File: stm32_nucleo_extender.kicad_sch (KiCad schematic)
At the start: 7 parts, among them CN10 6-534206-9, CN7 6-534206-9, J1 TBL009-254-20GY-2GY, J2 TBL009-254-20GY-2GY, J3 TBL009-254-20GY-2GY, J4 TBL009-254-20GY-2GY, U1 NUCLEO-F446RE

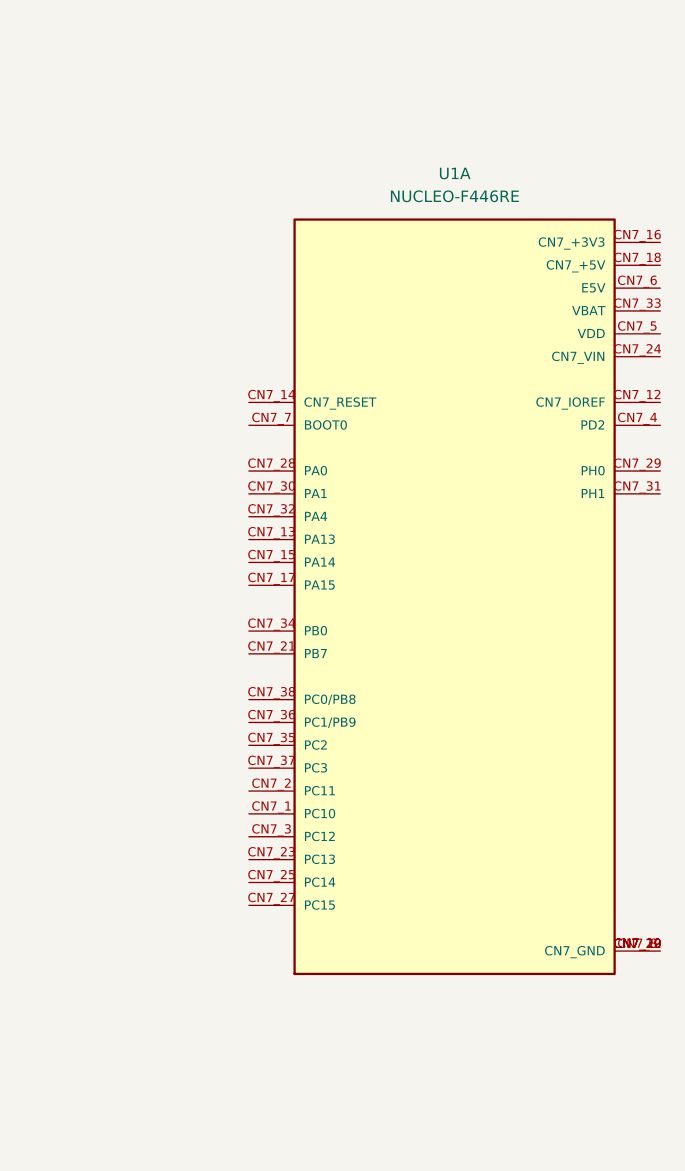
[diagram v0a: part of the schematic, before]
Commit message: [UPD] to kicad 10.0 [ADD] round tracks
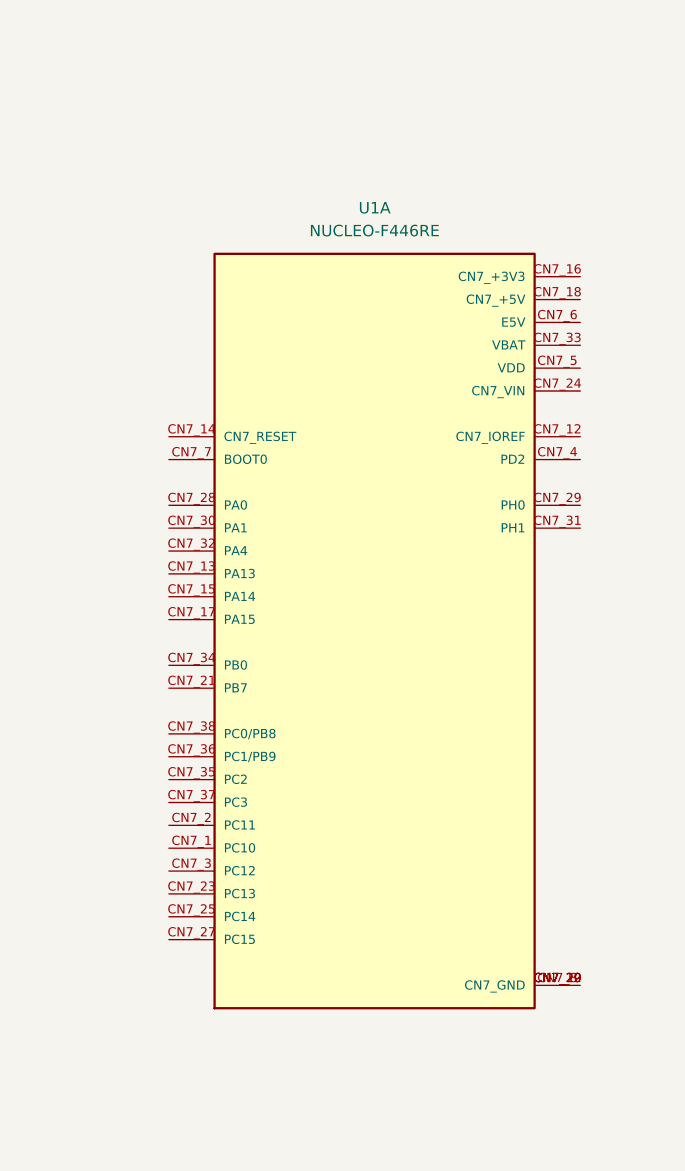
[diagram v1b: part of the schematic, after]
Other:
- moved on the sheet: U1A
